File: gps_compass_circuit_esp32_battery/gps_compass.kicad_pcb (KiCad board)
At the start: 2 copper layers, 80 x 46 mm, 41 parts, among them J1 USB_C_Receptacle_PowerOnly_6P, Q1 MMBTA92, U1 MCP1700x-330xxTT, U3 LTC4054ES5-4.2

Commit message: Aggiornamenti vari
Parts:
- removed the C3 at (140.0, 65.4)
- removed the C4 at (140.0, 69.5)
- removed L1: 120R@100Mhz, Inductor_SMD:L_0805_2012Metric_Pad1.15x1.40mm_HandSolder
- removed Oled1: display_oled, mia_libreria:Display_i2c_128x64
- removed lcd1: display_lcd, mia_libreria:display_7_segm_4_digits
- added LCD: Conn_01x05_Socket, mia_libreria:display_7_segm_4_digits, F.Cu at (129.5, 53.8)
- added Oled: Conn_01x04_Socket, mia_libreria:Display_i2c_128x64, F.Cu at (130.7, 57.3)
- GY-271: value Conn_01x05_Shielded -> Conn_01x05_Socket
- LED: renamed from LED1; moved to B.Cu
- Serial1: value Conn_01x03_Shielded -> Conn_01x03_Socket; moved to F.Cu
- moved R4 18.9 mm to (121.2, 62.8)
- moved Serial1 5.13 mm to (159.9, 33.3)
- moved En 4.10 mm to (113.7, 63.9)
- moved Prog 4.10 mm to (117.8, 63.9)
- moved ESP32 4.05 mm to (160.7, 74.2), turned to 180 degrees
- moved C7 2.56 mm to (135.1, 68.8)
- moved C6 2.56 mm to (135.1, 66.4)
- moved C3 1.61 mm to (121.2, 68.2)
- moved C4 1.61 mm to (121.2, 72.4)
- renumbered ESP32-S1 to ESP32-S, En1 to En, GPS1 to GPS, MAIN1 to MAIN, Prog1 to Prog, microsd1 to microsd
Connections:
- Serial1 pad 1: GND -> Net-(ESP32-S1-TXD0/IO1)
- Serial1 pad 3: Net-(ESP32-S1-TXD0/IO1) -> GND
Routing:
- net VCC: track 44.7 -> 76.7 mm, vias 2 -> 5
- net +3V3: track 47.2 -> 22.1 mm
- net Net-(ESP32-B): track 37.3 -> 30.5 mm, vias 1 -> 0
- net Net-(ESP32-S1-IO0): track 41.7 -> 36.5 mm
- net Net-(ESP32-S1-EN): track 45.6 -> 50.0 mm
- net Net-(MAIN1-B): track 9.24 -> 13.0 mm
- net Net-(GPS1-~{RESET}): track 11.5 -> 10.8 mm
- net lcd_cs: track 28.5 -> 27.9 mm
- net lcd_data: track 29.2 -> 28.7 mm
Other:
- board text added: "Dade3e 2023"
- board text added: "Esp32 GpsCompass"
- board text added: "Off"
- board text added: "On"

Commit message: Aggiornamenti vari
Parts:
- removed ESP32: SW_SPDT, Button_Switch_SMD:SW_SPDT_PCM12
- added ESP: SW_SPDT, Button_Switch_SMD:SW_SPDT_PCM12, B.Cu at (160.7, 74.2)
- added R10: 100K, Resistor_SMD:R_0603_1608Metric_Pad0.98x0.95mm_HandSolder, F.Cu at (118.1, 43.6)
- added R9: 27K, Resistor_SMD:R_0603_1608Metric_Pad0.98x0.95mm_HandSolder, F.Cu at (118.1, 47.2)
- moved R6 16.2 mm to (113.1, 46.5), turned to 180 degrees
- moved C5 13.0 mm to (135.5, 68.3), turned to 0 degrees
- moved C1 3.80 mm to (124.7, 61.5), turned to 180 degrees
- moved C6 3.13 mm to (135.5, 63.3)
- moved C7 3.13 mm to (135.5, 65.7)
- moved R5 2.86 mm to (125.6, 53.8)
- moved R3 1.69 mm to (122.9, 63.5)
- moved MAIN 1.54 mm to (129.6, 74.1)
- moved R7 1.27 mm to (110.8, 53.1), turned to -90 degrees
- moved U1 1.17 mm to (129.5, 64.0)
- moved R8 0.50 mm to (117.0, 53.9)
- moved SWb1 0.43 mm to (172.1, 66.2)
- moved J1 0.40 mm to (114.7, 56.5)
- renumbered LCD to LCD1, Oled to Oled1, microsd to microsd1
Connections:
- C5 pad 1: Net-(BT1-+) -> +BATT
- C6 pad 1: Net-(MAIN1-B) -> +3V3
- C7 pad 1: Net-(MAIN1-B) -> +3V3
- ESP32-S pad 9: unconnected-(ESP32-S1-IO33-Pad9) -> battery_level
- GPS pad 12: unconnected-(GPS1-SCL-Pad12) -> SCL
- MAIN pad 1: Net-(ESP32-B) -> +BATT
- MAIN pad 2: Net-(MAIN1-B) -> Net-(BT1-+)
- U1 pad 2: Net-(MAIN1-B) -> +3V3
- U1 pad 3: Net-(BT1-+) -> +BATT
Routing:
- net +3V3: track 22.1 -> 69.3 mm, vias 0 -> 1
- net battery_level: track 0.00 -> 37.0 mm, vias 0 -> 1
- net +BATT: track 0.00 -> 34.8 mm, vias 0 -> 1
- net VCC: track 76.7 -> 108.5 mm, vias 5 -> 4
- net Net-(ESP32-B): track 30.5 -> 0.00 mm
- net SCL: track 39.2 -> 69.7 mm
- net SDA: track 49.7 -> 67.0 mm
- net Net-(LED1-K): track 19.1 -> 2.41 mm
- net Net-(MAIN1-B): track 13.0 -> 0.00 mm
- net Net-(BT1-+): track 22.7 -> 31.7 mm
- net GND: track 0.00 -> 3.26 mm, vias 0 -> 1
- net Net-(ESP32-S1-EN): track 50.0 -> 52.8 mm
- net Net-(U3-VCC): track 25.9 -> 24.0 mm
- net MOSI: track 41.4 -> 42.4 mm
- net B2: track 30.5 -> 31.1 mm
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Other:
- board text added: "Walk, lose yourself, return"

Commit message: Riposizionati pulsanti
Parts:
- moved SWdown1 2.40 mm to (170.6, 56.6)
- moved SWb1 1.65 mm to (173.7, 66.2)
- moved SWa1 1.20 mm to (161.3, 66.2)
- moved SWleft1 1.20 mm to (161.3, 56.6)
- moved SWright1 1.20 mm to (161.3, 47.0)
- moved R1 0.80 mm to (145.2, 55.5)
- moved R2 0.80 mm to (147.0, 55.5)
- renumbered LCD1 to LCD, Oled1 to Oled
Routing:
- net B2: track 31.1 -> 35.2 mm
- net B6: track 49.7 -> 51.7 mm
- net B5: track 44.9 -> 46.5 mm
- net B4: track 29.3 -> 30.7 mm
- net B3: track 19.3 -> 20.5 mm
- net TX2: track 6.75 -> 7.71 mm
- net Net-(GPS1-RXD): track 18.1 -> 17.3 mm
- net Net-(GPS1-TXD): track 17.8 -> 17.0 mm
- net RX2: track 3.00 -> 3.80 mm

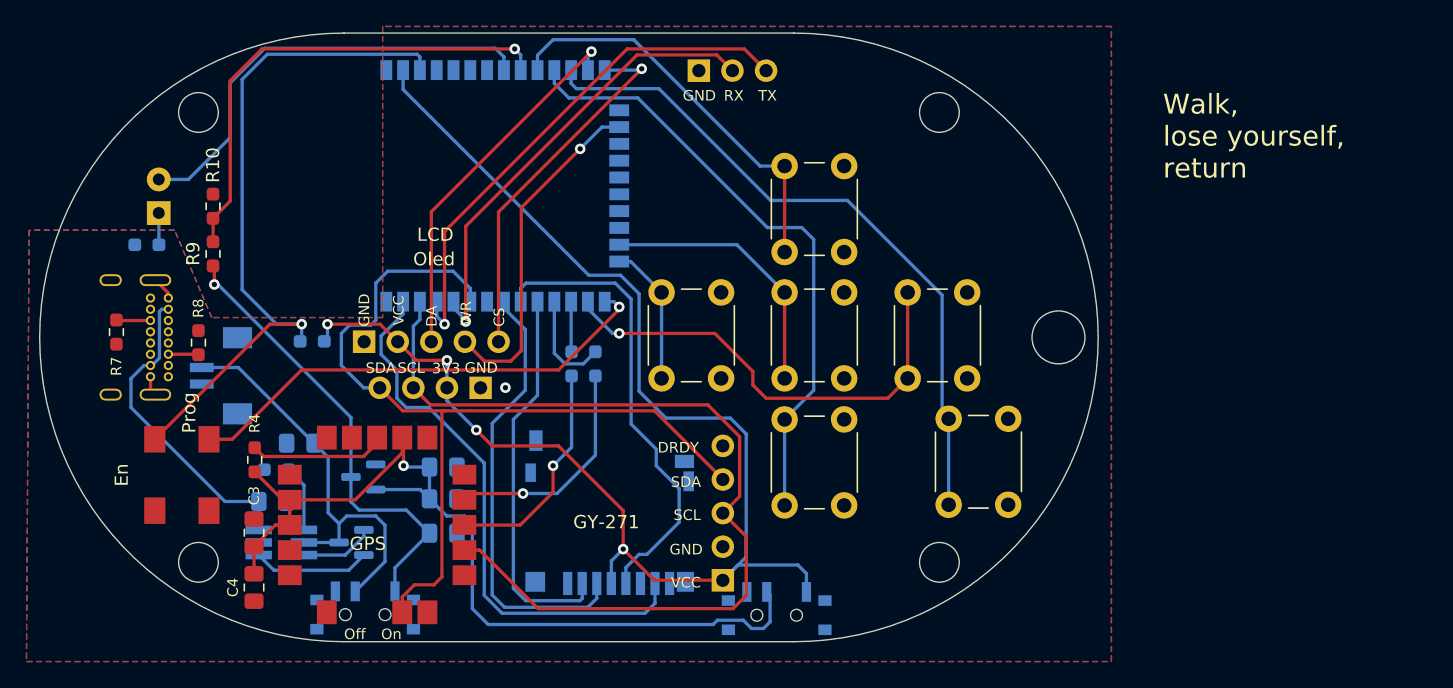
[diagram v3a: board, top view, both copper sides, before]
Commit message: Controllate piazzole GND
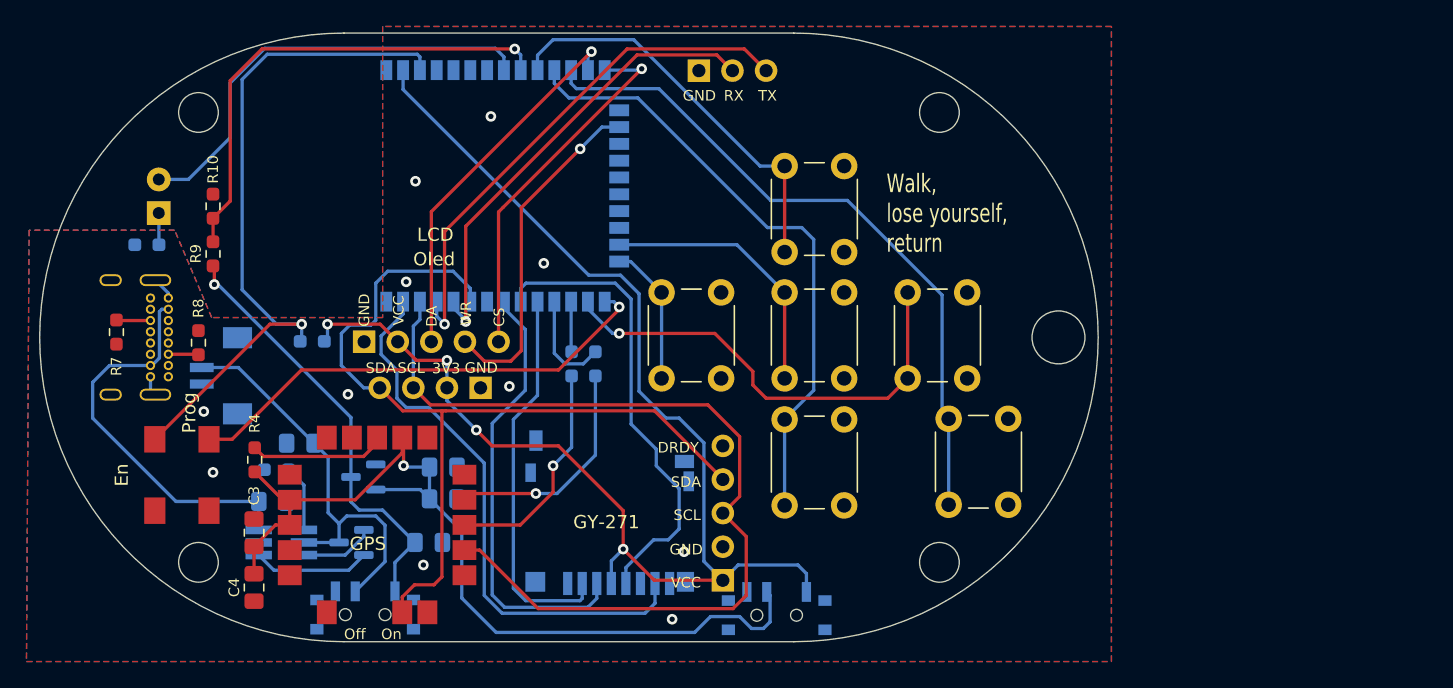
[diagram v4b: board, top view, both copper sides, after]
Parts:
- moved C5 1.30 mm to (134.4, 69.0)
- renumbered microsd1 to microsd
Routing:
- net Net-(U3-VCC): track 24.0 -> 30.1 mm
- net VCC: track 108.5 -> 104.8 mm
- net +BATT: track 34.8 -> 32.4 mm
- net GND: vias 1 -> 11
